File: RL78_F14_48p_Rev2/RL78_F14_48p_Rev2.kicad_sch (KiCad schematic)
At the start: 52 parts, among them P1 POWER_JACKPTH, P2 E2 Lite, P3 PWR, P4 ADC, P5 F09HP, P6 USB_B, P7 Keypad, P8 RPI LCD, P9 SPI_to_eth, U1 R5F10PGJKNA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

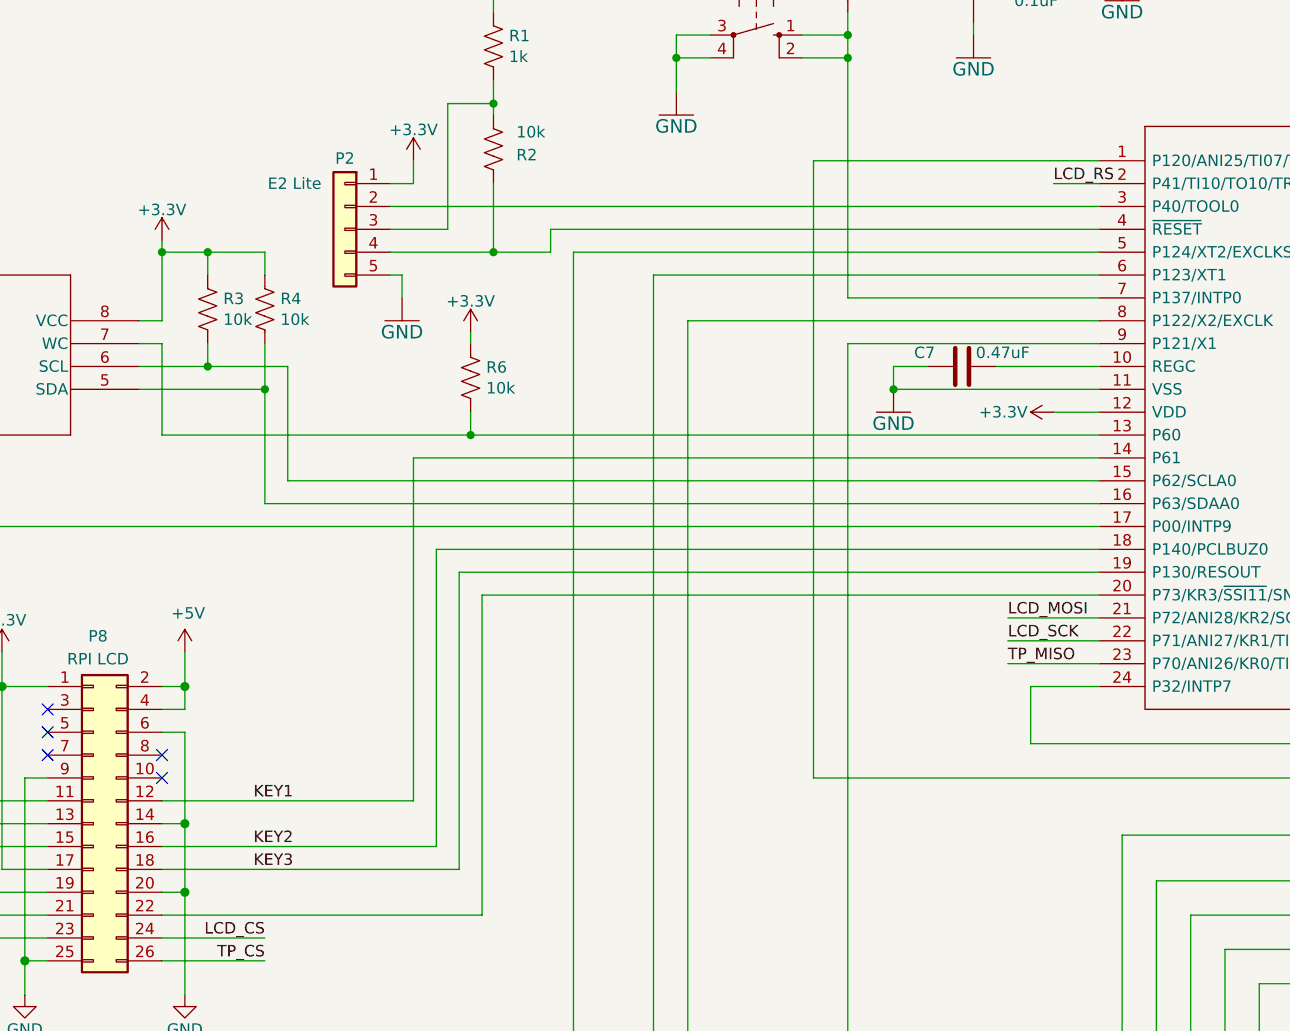
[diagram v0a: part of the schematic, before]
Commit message: OOPS! P130 is write only and I had it set as input for the LCD board
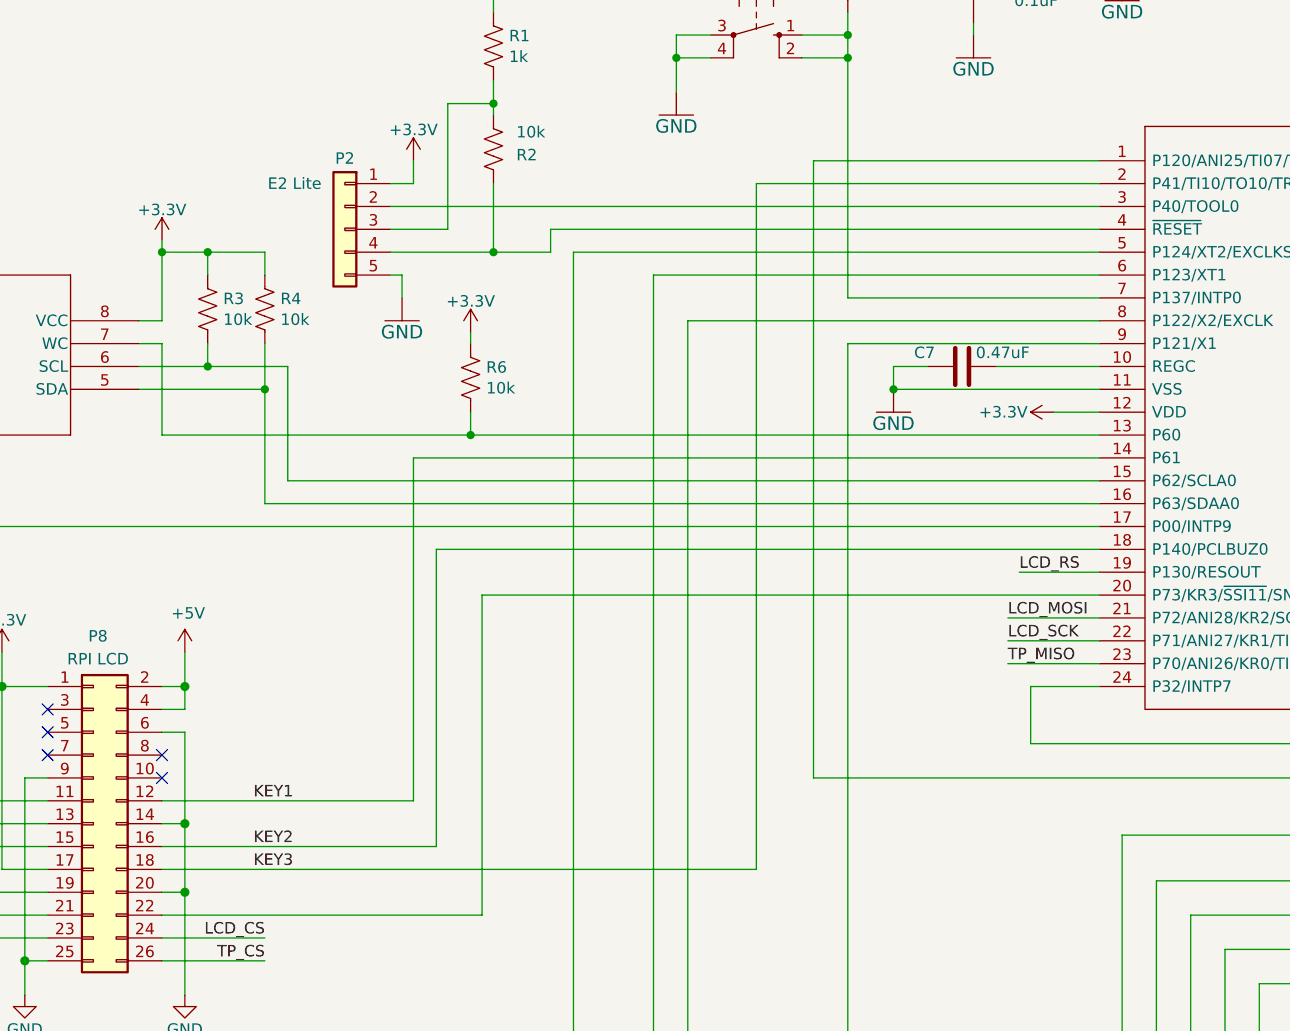
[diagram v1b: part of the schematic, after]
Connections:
- net KEY3: now also U1.2 (P41/TI10/TO10/TRJIO0/SNZOUT2); no longer U1.19 (P130/RESOUT)
- net LCD_RS: now also U1.19 (P130/RESOUT); no longer U1.2 (P41/TI10/TO10/TRJIO0/SNZOUT2)
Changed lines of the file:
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@@
-	(wire
-		(pts
-			(xy 106.68 137.16) (xy 177.8 137.16)
-		)
-		(stroke
-			(width 0)
-			(type default)
-		)
-	)
 	(wire
 		(pts
@@
 	(wire
 		(pts
-			(xy 73.66 170.18) (xy 106.68 170.18)
+			(xy 73.66 170.18) (xy 139.7 170.18)
 		)
 		(stroke
@@
 	(wire
 		(pts
-			(xy 177.8 93.98) (xy 172.72 93.98)
+			(xy 177.8 137.16) (xy 168.91 137.16)
 		)
 		(stroke
@@
 	(wire
 		(pts
-			(xy 106.68 137.16) (xy 106.68 170.18)
-		)
-		(stroke
-			(width 0)
-			(type default)
-		)
-	)
-	(wire
-		(pts
 			(xy 450.85 204.47) (xy 450.85 207.01)
 		)
@@
 	(wire
 		(pts
+			(xy 139.7 93.98) (xy 177.8 93.98)
+		)
+		(stroke
+			(width 0)
+			(type default)
+		)
+	)
+	(wire
+		(pts
 			(xy 325.12 252.73) (xy 420.37 252.73)
 		)
@@
 		(pts
 			(xy 420.37 252.73) (xy 420.37 247.65)
+		)
+		(stroke
+			(width 0)
+			(type default)
+		)
+	)
+	(wire
+		(pts
+			(xy 139.7 170.18) (xy 139.7 93.98)
 		)
 		(stroke
@@
 	)
 	(label "LCD_RS"
-		(at 172.72 93.98 0)
+		(at 168.91 137.16 0)
 		(fields_autoplaced yes)
 		(effects
